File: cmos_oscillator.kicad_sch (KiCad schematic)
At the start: 5 parts, among them X1 YC24.576MUBCE2O

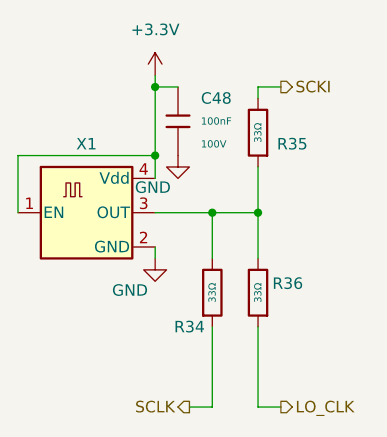
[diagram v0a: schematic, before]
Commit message: Editing 6 layer
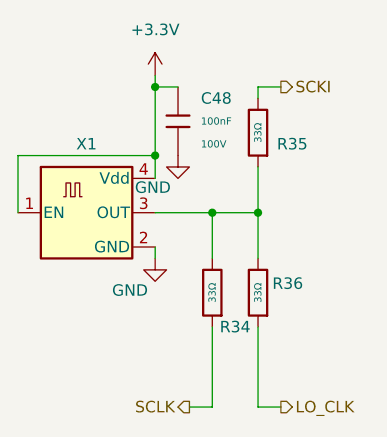
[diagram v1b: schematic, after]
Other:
- moved on the sheet: R34
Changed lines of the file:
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@@
 	(symbol
 		(lib_id "PCM_JLCPCB-Resistors:0805,33Ω")
-		(at 154.94 107.95 0)
-		(mirror x)
+		(at 154.94 107.95 180)
 		(unit 1)
 		(exclude_from_sim no)
@@
 		(dnp no)
 		(property "Reference" "R34"
-			(at 152.4 111.76 0)
+			(at 157.48 111.76 0)
 			(effects
 				(font
@@
 		)
 		(property "Footprint" "PCM_JLCPCB:R_0805"
-			(at 153.162 107.95 90)
+			(at 156.718 107.95 90)
 			(effects
 				(font
